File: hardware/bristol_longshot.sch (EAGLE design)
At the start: 42 parts, among them U1 SAM_D20E, U2 SI4060, U3 MAX1947, U4 ANTENOVA_GPS_M10382, U5 S25FS-S

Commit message: Board revision 0.96.0 sent
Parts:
- removed C20: 100pF, microbuilder_v3:CAP_CERAMIC_0402
- removed C21: 15pF, microbuilder_v3:CAP_CERAMIC_0402
- removed C22: DNP, microbuilder_v3:CAP_CERAMIC_0402
- removed C23: 4.7µF, resistor:C-EUC0603K
- removed R3, R4: 100Ω, microbuilder_v3:RESISTOR_0402
- removed U3: MAX1947, fbri:MAX1947
- added C4: 15pF, microbuilder_v3:CAP_CERAMIC_0402
- added ESD1, ESD2: 0.25pF, microbuilder_v3:FERRITE_0603MP
- added FB2: (no value), microbuilder_v3:FERRITE_0402
- added U$19: TPS3123, TPS3125:TPS3123
- added U$23: TG-5006CJ, fbri:TG-5006CJ
- added U$48: UBLOX_MAX, Ava:UBLOX_MAX
- C1: value 15pF -> 8.2pF
- C10, C8: value 8.2pF -> 100pF
- C13, C14, C15, C16: value 100pF -> 100nF
- C17: value 100pF -> 2.2µF
- C18: value 15pF -> 10µF; device microbuilder_v3:CAP_CERAMIC_0402 -> resistor:C-EUC0603K
- C19: value 100pF -> 10µF; device microbuilder_v3:CAP_CERAMIC_0402 -> resistor:C-EUC0603K
- C2: value 100nF -> 15pF
- C3: value 100nF -> 8.2pF
- C5, C6: value 2.2µF -> DNP
- C9: value 15pF -> 100pF
- L1: value 3.3µH -> 2.2µH
- R1: value 22Ω -> 100kΩ
- R2: value 100Ω -> 240kΩ
- U4: value ANTENOVA_GPS_M10382 -> ADP1607ACPZN-R7; device fbri:ANTENOVA_GPS_M10382 -> ADP1607:ADP1607ACPZN-R7
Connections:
- removed net AN_GPS_RX: C15.P$1, R4.1, U4.RX
- removed net AN_GPS_TX: R3.1, U4.TX
- removed net GPS_ANT_IN: C1.P$2, U4.ANT_IN
- removed net GPS_ANT_OUT: C1.P$1, U4.ANT_OUT
- removed net GPS_RX: R4.2, U1.PA00
- removed net GPS_TX: C16.P$1, R3.2, U1.PA01
- removed net LED_RES: D1.C, R1.2
- removed net LX: L1.1, U3.LX
- removed net N$1: C20.P$1, U$2.+2
- removed net RESETN: JTAG1.10, U1.PA05, U1.PA15, U1.RESETN, U3.NRST
- removed net SI_HF_CLK: U1.PA17, U2.XIN
- removed net TIME_1KHZ: C13.P$1, R2.1, U1.PA28
- removed net TIME_1KHZ_DRIVE: R2.2, U4.TIMEPULSE/TDO
- new net !RESET: U$19.!RESET, U1.RESETN
- new net FB: R1.1, R2.2, U4.FB
- new net GIMO: U$48.3_RXD1, U1.PA00
- new net GOMI: U$48.2_TXD1, U1.PA01
- new net GPS_ANT: ESD1.P$2, U$48.11_RF_IN
- new net LED: D1.C, U1.PA15
- new net RADIO_XIN: C13.P$2, U2.XIN
- new net SW: L1.2, U4.SW
- new net TCXO_OUT: C13.P$1, U$23.OUT, U1.PA17
- new net TCXO_VDD: C12.P$1, FB2.P$1, U$23.VCC
- new net TIMEPULSE: U$48.4_TIMEPULSE, U1.PA05
- new net WDI: U$19.WDI, U1.PA28
- net 1.2V: now also C18.1, L1.1, U4.EN, U4.VIN; no longer C14.P$1, C5.P$1, L1.2, U3.BATT, U3.NSHDN
- net 1.8V: now also C10.P$1, C14.P$1, C15.P$1, C19.1, C9.P$1, FB2.P$2, R1.2, U$19.!MR, U$19.VDD, U$48.7_VCC_IO, U$48.8_VCC, U4.VOUT; no longer C12.P$1, C19.P$1, C23.1, C3.P$1, U3.OUT, U4.VCC, U4.VDD_RF, U4.VIO
- net ANT: now also C1.P$1, ESD2.P$2; no longer C10.P$1
- net FILTER1: now also C3.P$1, C6.P$1; no longer C22.P$1, C8.P$1
- net FILTER2: now also C2.P$1; no longer C9.P$1
- net GND: now also C1.P$2, C18.2, C19.2, C7.P$2, ESD1.P$1, ESD2.P$1, R2.1, U$19.GND, U$23.GND, U$48.10_GND, U$48.12_GND, U$48.1_GND, U4.EP, U4.GND; no longer C13.P$2, C18.P$2, C19.P$2, C20.P$2, C21.P$1, C23.2, C6.P$2, U3.GNDA, U3.GNDB, U3.GND_PAD, U3.PGND, U4.GND1, U4.GND10, U4.GND11, U4.GND12, U4.GND2, U4.GND3, U4.GND4, U4.GND5, U4.GND6, U4.GND7, U4.GND8, U4.GND9, U4.VDD_USB
- net RADIO_VDD: now also C7.P$1, C8.P$1; no longer C18.P$1, C6.P$1
- net RF_OUT: now also C4.P$2; no longer C7.P$2
- net RXN: now also C5.P$1; no longer C21.P$2
- net RXP: now also C6.P$2; no longer C22.P$2
- net SI_GPIO0: no longer R1.1
- net TANK: now also C4.P$1; no longer C7.P$1
- net VDD_CORE: now also C16.P$1; no longer C2.P$1
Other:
- note added: "(0.8V p-p min)"
- note added: "(GLCK_IO[3])"
- note added: "(TC0 WC[1])"
- note added: "ADP1607 Step-Up DC-DC Converter VBatt -> 1.8V"
- note added: "MAX8C GPS"
- note removed: "(GCLK_IO[0])"
- note removed: "(GCLK_IO[3])"
- note removed: "Antenova M10382 GPS Module, U-Blox 6 Chipset"
- note removed: "Datasheet suggests both 18pF and 22pF"
- note removed: "MAX1947 Step-Up DC-DC Converter VBatt -> 1.8V"
- moved on the sheet: C1, C10, C12, C13, C14, C15, C16, C17, C18, C19, C2, C3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

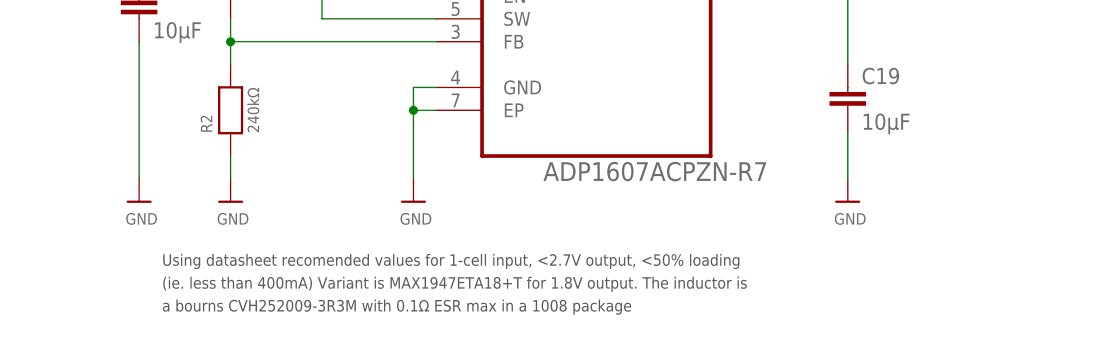
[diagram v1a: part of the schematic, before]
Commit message: Removed out of data dc-dc converter notes
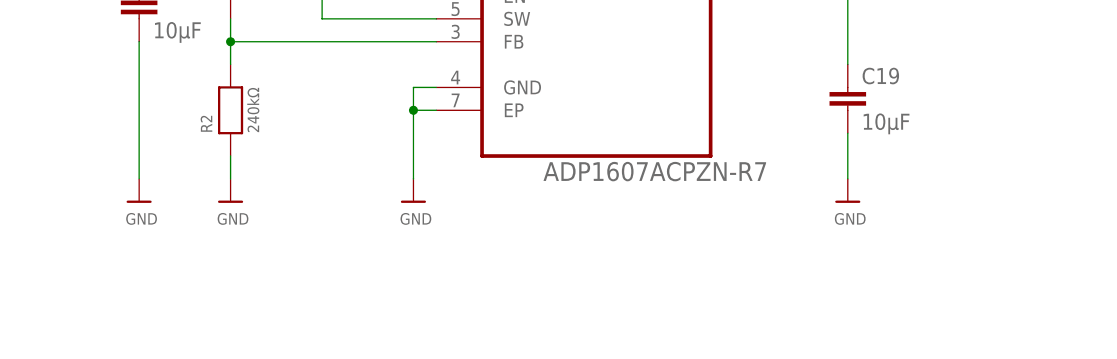
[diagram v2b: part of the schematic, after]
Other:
- note removed: "Using datasheet recomended values for 1-cell input, <2.7V output, <50% loading (ie. less than 400mA) Variant is MAX1947ETA18+T for 1.8V output. The inductor is a bourns CVH252009-3R3M with 0.1Ω ESR max in a 1008 package"
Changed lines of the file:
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@@
 <text x="99.06" y="138.684" size="1.27" layer="97" font="vector" ratio="11" rot="MR0">(SWD)</text>
 <wire x1="100.076" y1="141.224" x2="100.076" y2="136.652" width="0.1524" layer="97"/>
-<text x="43.18" y="18.288" size="1.27" layer="97" font="vector" ratio="11" distance="100">Using datasheet recomended values for 1-cell input, &lt;2.7V output, &lt;50% loading
-(ie. less than 400mA) Variant is MAX1947ETA18+T for 1.8V output. The inductor is
-a bourns CVH252009-3R3M with 0.1Ω ESR max in a 1008 package</text>
 <text x="93.98" y="117.094" size="1.27" layer="97" font="vector" ratio="11" rot="MR0">(SERCOM0)</text>
 <wire x1="94.996" y1="118.364" x2="94.996" y2="113.792" width="0.1524" layer="97"/>

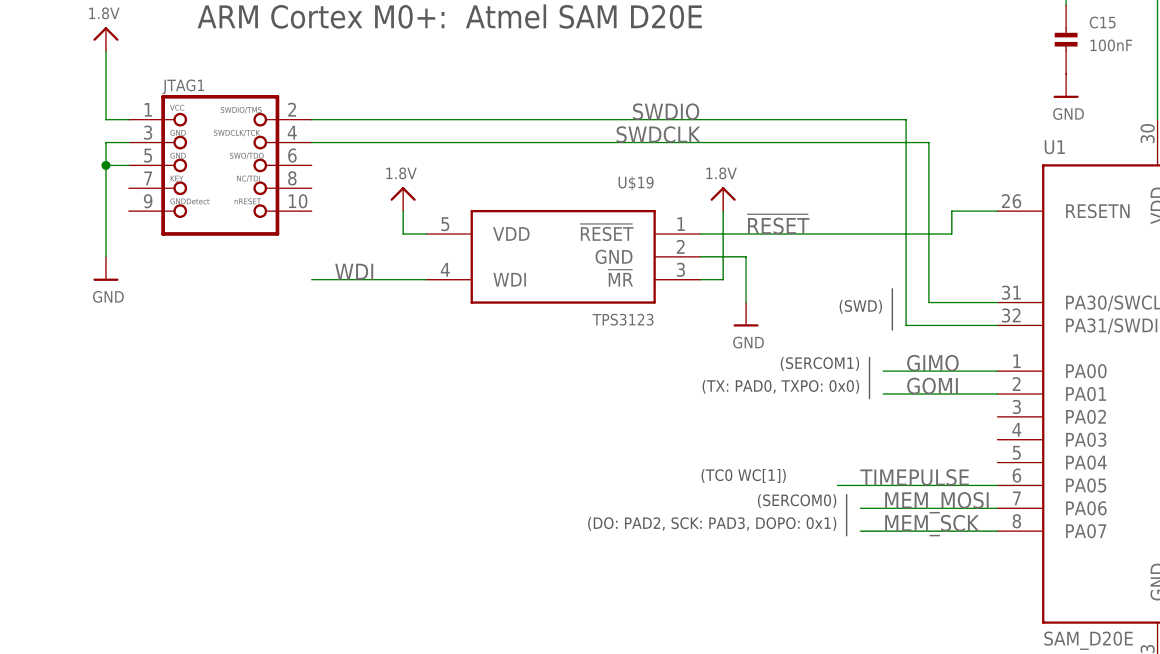
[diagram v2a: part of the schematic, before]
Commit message: Added !MR link to cortex debug connex, allows programming but not debugging of boards with watchdog enabled
Boards with watchdogs mounted can be programmed by holding !MR low. On blackmagic `mon conn e`
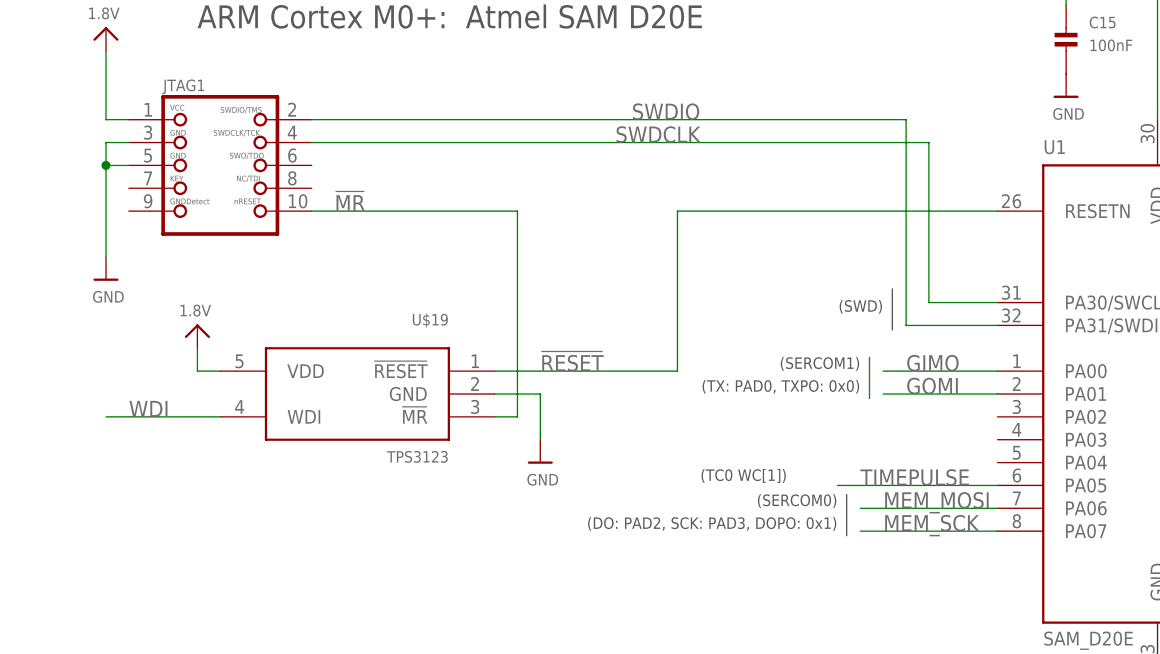
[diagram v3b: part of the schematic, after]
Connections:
- new net !MR: JTAG1.10, U$19.!MR
- net 1.8V: no longer U$19.!MR
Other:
- moved on the sheet: U$19
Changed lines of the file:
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@@
 <?xml version="1.0" encoding="utf-8"?>
 <!DOCTYPE eagle SYSTEM "eagle.dtd">
-<eagle version="6.6.0">
+<eagle version="6.5.0">
 <drawing>
 <settings>
@@
 <part name="U$20" library="microbuilder_v3" deviceset="1.8V" device=""/>
 <part name="U$21" library="microbuilder_v3" deviceset="GND" device=""/>
-<part name="U$22" library="microbuilder_v3" deviceset="1.8V" device=""/>
 <part name="U$23" library="fbri" deviceset="TG-5006CJ" device=""/>
 <part name="U$24" library="microbuilder_v3" deviceset="1.8V" device=""/>
@@
 <instance part="U$18" gate="G$1" x="381" y="53.34"/>
 <instance part="C10" gate="G$1" x="165.1" y="58.42"/>
-<instance part="U$19" gate="A" x="63.5" y="144.78" rot="MR0"/>
-<instance part="U$20" gate="G$1" x="45.72" y="152.4" rot="MR0"/>
-<instance part="U$21" gate="G$1" x="83.82" y="137.16"/>
-<instance part="U$22" gate="G$1" x="81.28" y="152.4" rot="MR0"/>
+<instance part="U$19" gate="A" x="40.64" y="129.54" rot="MR0"/>
+<instance part="U$20" gate="G$1" x="22.86" y="137.16" rot="MR0"/>
+<instance part="U$21" gate="G$1" x="60.96" y="121.92"/>
 <instance part="U$23" gate="A" x="304.8" y="139.7"/>
 <instance part="U$24" gate="G$1" x="287.02" y="160.02" rot="MR0"/>
@@
 <segment>
 <pinref part="U$21" gate="G$1" pin="GND"/>
-<wire x1="83.82" y1="144.78" x2="83.82" y2="139.7" width="0.1524" layer="91"/>
+<wire x1="60.96" y1="129.54" x2="60.96" y2="124.46" width="0.1524" layer="91"/>
 <pinref part="U$19" gate="A" pin="GND"/>
-<wire x1="78.74" y1="144.78" x2="83.82" y2="144.78" width="0.1524" layer="91"/>
+<wire x1="55.88" y1="129.54" x2="60.96" y2="129.54" width="0.1524" layer="91"/>
 </segment>
 <segment>
@@
 <segment>
 <pinref part="U$20" gate="G$1" pin="1.8V"/>
-<wire x1="45.72" y1="147.32" x2="45.72" y2="149.86" width="0.1524" layer="91"/>
+<wire x1="22.86" y1="132.08" x2="22.86" y2="134.62" width="0.1524" layer="91"/>
 <pinref part="U$19" gate="A" pin="VDD"/>
-<wire x1="48.26" y1="147.32" x2="45.72" y2="147.32" width="0.1524" layer="91"/>
-</segment>
-<segment>
-<pinref part="U$19" gate="A" pin="!MR"/>
-<pinref part="U$22" gate="G$1" pin="1.8V"/>
-<wire x1="78.74" y1="142.24" x2="81.28" y2="142.24" width="0.1524" layer="91"/>
-<wire x1="81.28" y1="142.24" x2="81.28" y2="149.86" width="0.1524" layer="91"/>
+<wire x1="25.4" y1="132.08" x2="22.86" y2="132.08" width="0.1524" layer="91"/>
 </segment>
 <segment>
@@
 <net name="!RESET" class="0">
 <segment>
+<pinref part="U$19" gate="A" pin="!RESET"/>
+<wire x1="76.2" y1="132.08" x2="55.88" y2="132.08" width="0.1524" layer="91"/>
+<label x="60.96" y="132.08" size="1.778" layer="95"/>
+<wire x1="76.2" y1="132.08" x2="76.2" y2="149.86" width="0.1524" layer="91"/>
 <pinref part="U1" gate="G$1" pin="RESETN"/>
-<pinref part="U$19" gate="A" pin="!RESET"/>
-<wire x1="111.76" y1="149.86" x2="106.68" y2="149.86" width="0.1524" layer="91"/>
-<wire x1="106.68" y1="149.86" x2="106.68" y2="147.32" width="0.1524" layer="91"/>
-<wire x1="106.68" y1="147.32" x2="78.74" y2="147.32" width="0.1524" layer="91"/>
-<label x="83.82" y="147.32" size="1.778" layer="95"/>
+<wire x1="76.2" y1="149.86" x2="111.76" y2="149.86" width="0.1524" layer="91"/>
 </segment>
 </net>
@@
 <segment>
 <pinref part="U$19" gate="A" pin="WDI"/>
-<wire x1="48.26" y1="142.24" x2="35.56" y2="142.24" width="0.1524" layer="91"/>
-<label x="38.1" y="142.24" size="1.778" layer="95"/>
+<wire x1="25.4" y1="127" x2="12.7" y2="127" width="0.1524" layer="91"/>
+<label x="15.24" y="127" size="1.778" layer="95"/>
 </segment>
 <segment>
@@
 </segment>
 </net>
+<net name="!MR" class="0">
+<segment>
+<pinref part="U$19" gate="A" pin="!MR"/>
+<wire x1="55.88" y1="127" x2="58.42" y2="127" width="0.1524" layer="91"/>
+<pinref part="JTAG1" gate="G$1" pin="10"/>
+<wire x1="35.56" y1="149.86" x2="58.42" y2="149.86" width="0.1524" layer="91"/>
+<wire x1="58.42" y1="149.86" x2="58.42" y2="127" width="0.1524" layer="91"/>
+<label x="38.1" y="149.86" size="1.778" layer="95"/>
+</segment>
+</net>

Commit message: Merge
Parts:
- added JP1: (no value), SparkFun:M04LOCK
- added JP2: (no value), SparkFun:M06LOCK
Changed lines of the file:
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@@
 <part name="ESD2" library="microbuilder_v3" deviceset="FERRITE" device="_0603MP" value="0.25pF"/>
 <part name="U$31" library="microbuilder_v3" deviceset="GND" device=""/>
+<part name="JP1" library="SparkFun" deviceset="M04" device="LOCK"/>
+<part name="JP2" library="SparkFun" deviceset="M06" device="LOCK"/>
 </parts>
 <sheets>
@@
 <instance part="ESD2" gate="G$1" x="281.94" y="104.14" rot="R90"/>
 <instance part="U$31" gate="G$1" x="281.94" y="93.98"/>
+<instance part="JP1" gate="G$1" x="447.04" y="152.4" rot="R180"/>
+<instance part="JP2" gate="G$1" x="459.74" y="129.54" rot="R180"/>
 </instances>
 <busses>

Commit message: Rocketry board layout complete, todo: Adjust buck reference for higher vcc
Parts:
- added R3, R4: 10kΩ, microbuilder_v3:RESISTOR_0402
- JP1: device SparkFun:M04LOCK -> SparkFun:M06LOCK
- JP2: device SparkFun:M06LOCK -> SparkFun:M04LOCK
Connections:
- removed net TIMEPULSE: U$48.4_TIMEPULSE, U1.PA05
- new net SCL: JP1.2, JP2.1, R3.1, U1.PA05
- new net SDA: JP1.1, JP2.2, R4.1, U1.PA04
- net 1.8V: now also JP1.6, JP2.4, R3.2, R4.2
- net GND: now also JP1.5, JP2.3
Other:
- note removed: "(TC0 WC[1])"
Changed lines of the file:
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@@
 <part name="ESD2" library="microbuilder_v3" deviceset="FERRITE" device="_0603MP" value="0.25pF"/>
 <part name="U$31" library="microbuilder_v3" deviceset="GND" device=""/>
-<part name="JP1" library="SparkFun" deviceset="M04" device="LOCK"/>
-<part name="JP2" library="SparkFun" deviceset="M06" device="LOCK"/>
+<part name="JP1" library="SparkFun" deviceset="M06" device="LOCK"/>
+<part name="JP2" library="SparkFun" deviceset="M04" device="LOCK"/>
+<part name="U$22" library="microbuilder_v3" deviceset="GND" device=""/>
+<part name="U$38" library="microbuilder_v3" deviceset="1.8V" device=""/>
+<part name="U$51" library="microbuilder_v3" deviceset="GND" device=""/>
+<part name="U$54" library="microbuilder_v3" deviceset="1.8V" device=""/>
+<part name="R3" library="microbuilder_v3" deviceset="RESISTOR" device="_0402" value="10kΩ"/>
+<part name="R4" library="microbuilder_v3" deviceset="RESISTOR" device="_0402" value="10kΩ"/>
+<part name="U$59" library="microbuilder_v3" deviceset="1.8V" device=""/>
+<part name="U$60" library="microbuilder_v3" deviceset="1.8V" device=""/>
 </parts>
 <sheets>
@@
 connection on the
 holder</text>
-<text x="78.74" y="119.888" size="1.27" layer="97" font="vector" ratio="11">(TC0 WC[1])</text>
 <text x="170.18" y="132.588" size="1.27" layer="97" font="vector" ratio="11">(GLCK_IO[3])</text>
 <text x="185.42" y="132.588" size="1.27" layer="97" font="vector" ratio="11">(0.8V p-p min)</text>
+<wire x1="94.996" y1="123.444" x2="94.996" y2="118.872" width="0.1524" layer="97"/>
+<text x="93.98" y="122.174" size="1.27" layer="97" font="vector" ratio="11" rot="MR0">(SERCOM0)</text>
+<text x="93.98" y="119.634" size="1.27" layer="97" font="vector" ratio="11" rot="MR0">(TX: PAD0, TXPO: 0x0)</text>
 </plain>
 <instances>
@@
 <instance part="ESD2" gate="G$1" x="281.94" y="104.14" rot="R90"/>
 <instance part="U$31" gate="G$1" x="281.94" y="93.98"/>
-<instance part="JP1" gate="G$1" x="447.04" y="152.4" rot="R180"/>
-<instance part="JP2" gate="G$1" x="459.74" y="129.54" rot="R180"/>
+<instance part="JP1" gate="G$1" x="480.06" y="111.76" rot="MR0"/>
+<instance part="JP2" gate="G$1" x="480.06" y="137.16" rot="MR0"/>
+<instance part="U$22" gate="G$1" x="462.28" y="116.84" rot="R270"/>
+<instance part="U$38" gate="G$1" x="462.28" y="127" rot="MR0"/>
+<instance part="U$51" gate="G$1" x="462.28" y="139.7" rot="R270"/>
+<instance part="U$54" gate="G$1" x="462.28" y="149.86" rot="MR0"/>
+<instance part="R3" gate="G$1" x="452.12" y="116.84" rot="R90"/>
+<instance part="R4" gate="G$1" x="444.5" y="116.84" rot="R90"/>
+<instance part="U$59" gate="G$1" x="452.12" y="127" rot="MR0"/>
+<instance part="U$60" gate="G$1" x="444.5" y="127" rot="MR0"/>
 </instances>
 <busses>
@@
 <wire x1="281.94" y1="96.52" x2="281.94" y2="101.6" width="0.1524" layer="91"/>
 </segment>
+<segment>
+<pinref part="JP1" gate="G$1" pin="5"/>
+<wire x1="474.98" y1="116.84" x2="464.82" y2="116.84" width="0.1524" layer="91"/>
+<pinref part="U$22" gate="G$1" pin="GND"/>
+</segment>
+<segment>
+<pinref part="JP2" gate="G$1" pin="3"/>
+<pinref part="U$51" gate="G$1" pin="GND"/>
+<wire x1="464.82" y1="139.7" x2="474.98" y2="139.7" width="0.1524" layer="91"/>
+</segment>
 </net>
 <net name="SWDIO" class="0">
@@
 <pinref part="U$24" gate="G$1" pin="1.8V"/>
 <wire x1="287.02" y1="154.94" x2="287.02" y2="157.48" width="0.1524" layer="91"/>
+</segment>
+<segment>
+<pinref part="JP1" gate="G$1" pin="6"/>
+<wire x1="474.98" y1="119.38" x2="462.28" y2="119.38" width="0.1524" layer="91"/>
+<label x="467.36" y="119.38" size="1.778" layer="95"/>
+<pinref part="U$38" gate="G$1" pin="1.8V"/>
+<wire x1="462.28" y1="119.38" x2="462.28" y2="124.46" width="0.1524" layer="91"/>
+</segment>
+<segment>
+<pinref part="JP2" gate="G$1" pin="4"/>
+<pinref part="U$54" gate="G$1" pin="1.8V"/>
+<wire x1="474.98" y1="142.24" x2="462.28" y2="142.24" width="0.1524" layer="91"/>
+<wire x1="462.28" y1="142.24" x2="462.28" y2="147.32" width="0.1524" layer="91"/>
+<label x="467.36" y="142.24" size="1.778" layer="95"/>
+</segment>
+<segment>
+<pinref part="R4" gate="G$1" pin="2"/>
+<pinref part="U$60" gate="G$1" pin="1.8V"/>
+<wire x1="444.5" y1="124.46" x2="444.5" y2="121.92" width="0.1524" layer="91"/>
+</segment>
+<segment>
+<pinref part="R3" gate="G$1" pin="2"/>
+<pinref part="U$59" gate="G$1" pin="1.8V"/>
+<wire x1="452.12" y1="124.46" x2="452.12" y2="121.92" width="0.1524" layer="91"/>
 </segment>
 </net>
@@
 </segment>
 </net>
-<net name="TIMEPULSE" class="0">
-<segment>
-<label x="355.6" y="38.1" size="1.778" layer="95" ratio="11"/>
-<wire x1="373.38" y1="38.1" x2="350.52" y2="38.1" width="0.1524" layer="91"/>
-<pinref part="U$48" gate="G$1" pin="4_TIMEPULSE"/>
-</segment>
-<segment>
-<pinref part="U1" gate="G$1" pin="PA05"/>
-<wire x1="111.76" y1="119.38" x2="93.98" y2="119.38" width="0.1524" layer="91"/>
-<label x="96.52" y="119.38" size="1.778" layer="95"/>
-</segment>
-</net>
 <net name="GOMI" class="0">
 <segment>
@@
 </segment>
 </net>
+<net name="SCL" class="0">
+<segment>
+<pinref part="U1" gate="G$1" pin="PA05"/>
+<wire x1="111.76" y1="119.38" x2="109.22" y2="119.38" width="0.1524" layer="91"/>
+<wire x1="96.52" y1="119.38" x2="106.68" y2="119.38" width="0.1524" layer="91"/>
+<wire x1="106.68" y1="119.38" x2="109.22" y2="119.38" width="0.1524" layer="91"/>
+<label x="99.06" y="119.38" size="1.778" layer="95"/>
+</segment>
+<segment>
+<pinref part="JP1" gate="G$1" pin="2"/>
+<label x="467.36" y="109.22" size="1.778" layer="95"/>
+<pinref part="R3" gate="G$1" pin="1"/>
+<wire x1="452.12" y1="111.76" x2="452.12" y2="109.22" width="0.1524" layer="91"/>
+<wire x1="464.82" y1="109.22" x2="474.98" y2="109.22" width="0.1524" layer="91"/>
+<wire x1="464.82" y1="109.22" x2="452.12" y2="109.22" width="0.1524" layer="91"/>
+</segment>
+<segment>
+<pinref part="JP2" gate="G$1" pin="1"/>
+<wire x1="474.98" y1="134.62" x2="464.82" y2="134.62" width="0.1524" layer="91"/>
+<label x="467.36" y="134.62" size="1.778" layer="95"/>
+</segment>
+</net>
+<net name="SDA" class="0">
+<segment>
+<pinref part="U1" gate="G$1" pin="PA04"/>
+<wire x1="111.76" y1="121.92" x2="96.52" y2="121.92" width="0.1524" layer="91"/>
+<label x="99.06" y="121.92" size="1.778" layer="95"/>
+</segment>
+<segment>
+<pinref part="JP1" gate="G$1" pin="1"/>
+<label x="467.36" y="106.68" size="1.778" layer="95"/>
+<pinref part="R4" gate="G$1" pin="1"/>
+<wire x1="474.98" y1="106.68" x2="444.5" y2="106.68" width="0.1524" layer="91"/>
+<wire x1="444.5" y1="106.68" x2="444.5" y2="111.76" width="0.1524" layer="91"/>
+</segment>
+<segment>
+<pinref part="JP2" gate="G$1" pin="2"/>
+<wire x1="474.98" y1="137.16" x2="464.82" y2="137.16" width="0.1524" layer="91"/>
+<label x="467.36" y="137.16" size="1.778" layer="95"/>
+</segment>
+</net>
